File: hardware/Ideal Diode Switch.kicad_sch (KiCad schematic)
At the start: 49 parts, among them J9 Conn_01x12, Q10 SIR880BDP, Q11 SIR880BDP, Q12 SIR880BDP, Q5 SIR880BDP, Q6 SIR880BDP, Q7 SIR880BDP, Q8 SIR880BDP, Q9 SIR880BDP, U2 LM74810QDRRRQ1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

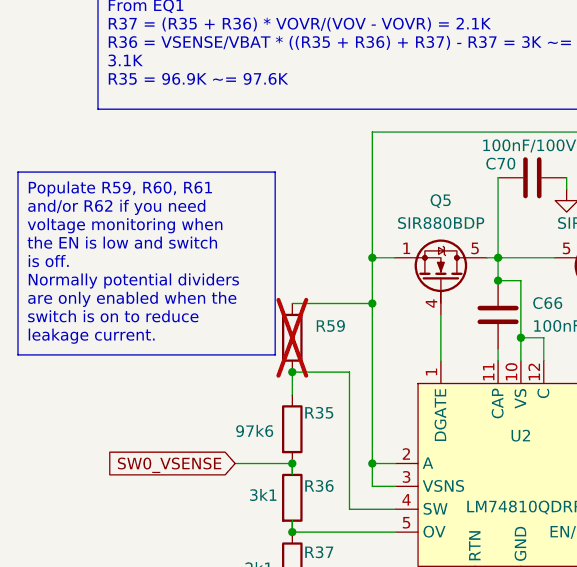
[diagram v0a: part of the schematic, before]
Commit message: Update to the title block
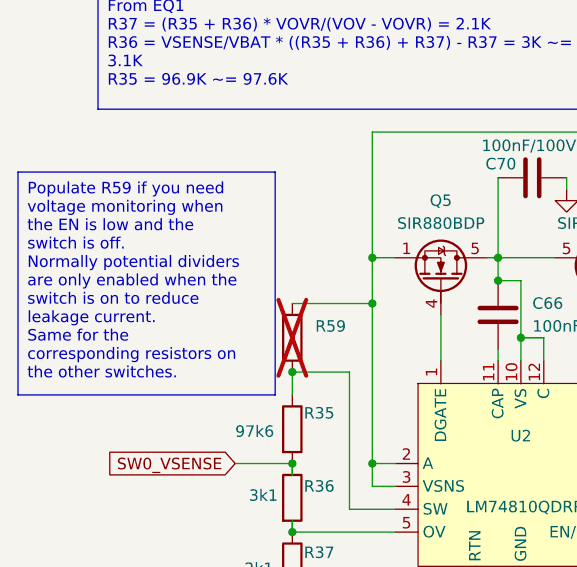
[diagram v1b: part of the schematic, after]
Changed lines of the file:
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@@
 	(paper "A4")
 	(title_block
-		(date "2025-11-07")
+		(date "2025-11-24")
 		(rev "1.0")
 		(company "Open Source Solutions Pty Ltd")
@@
 		)
 	)
-	(text_box "Populate R59, R60, R61 and/or R62 if you need voltage monitoring when the EN is low and switch is off.\nNormally potential dividers are only enabled when the switch is on to reduce leakage current."
+	(text_box "Populate R59 if you need voltage monitoring when the EN is low and the switch is off.\nNormally potential dividers are only enabled when the switch is on to reduce leakage current.\nSame for the corresponding resistors on the other switches."
 		(exclude_from_sim no)
 		(at 13.97 51.435 0)
-		(size 28.575 20.32)
-		(stroke
-			(width 0)
+		(size 28.575 24.765)
+		(stroke
+			(width 0)
